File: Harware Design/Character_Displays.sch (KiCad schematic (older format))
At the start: 53 parts, among them P10 CONN_01X01, P11 CONN_01X01, P12 CONN_01X01, P13 CONN_01X04, P14 CONN_01X01, P15 CONN_01X01, P17 CONN_01X16, P18 CONN_01X16, P20 CONN_01X01, P21 CONN_01X08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

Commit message: Changed design files as per issues
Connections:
- net MISO: now also SD1.7 (DATA0); no longer U5.3 (1Y)
- net at U5.2 (1A): no longer SD1.7 (DATA0)
- no-connect marks 8 -> 10
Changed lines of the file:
@@
 Text GLabel 5900 3850 0    40   Input ~ 0
 SCK
-Wire Wire Line
-	7900 4100 7600 4100
-Wire Wire Line
-	7600 4100 7600 4500
-Wire Wire Line
-	7600 4500 5650 4500
-Wire Wire Line
-	5650 3550 6000 3550
-Text GLabel 5900 3650 0    40   Input ~ 0
+Text GLabel 7900 4100 0    40   Input ~ 0
 MISO
 $Comp
@@
 	6900 3550 6800 3550
 Connection ~ 6900 3850
-Wire Wire Line
-	5900 3650 6000 3650
 Wire Wire Line
 	5950 3450 6000 3450
@@
 Wire Wire Line
 	7050 3350 7050 3400
-Wire Wire Line
-	5650 4500 5650 3550
 $Comp
 L CONN_01X01 P20
@@
 $EndComp
 NoConn ~ 7700 6250
+NoConn ~ 6000 3550
+NoConn ~ 6000 3650
 $EndSCHEMATC

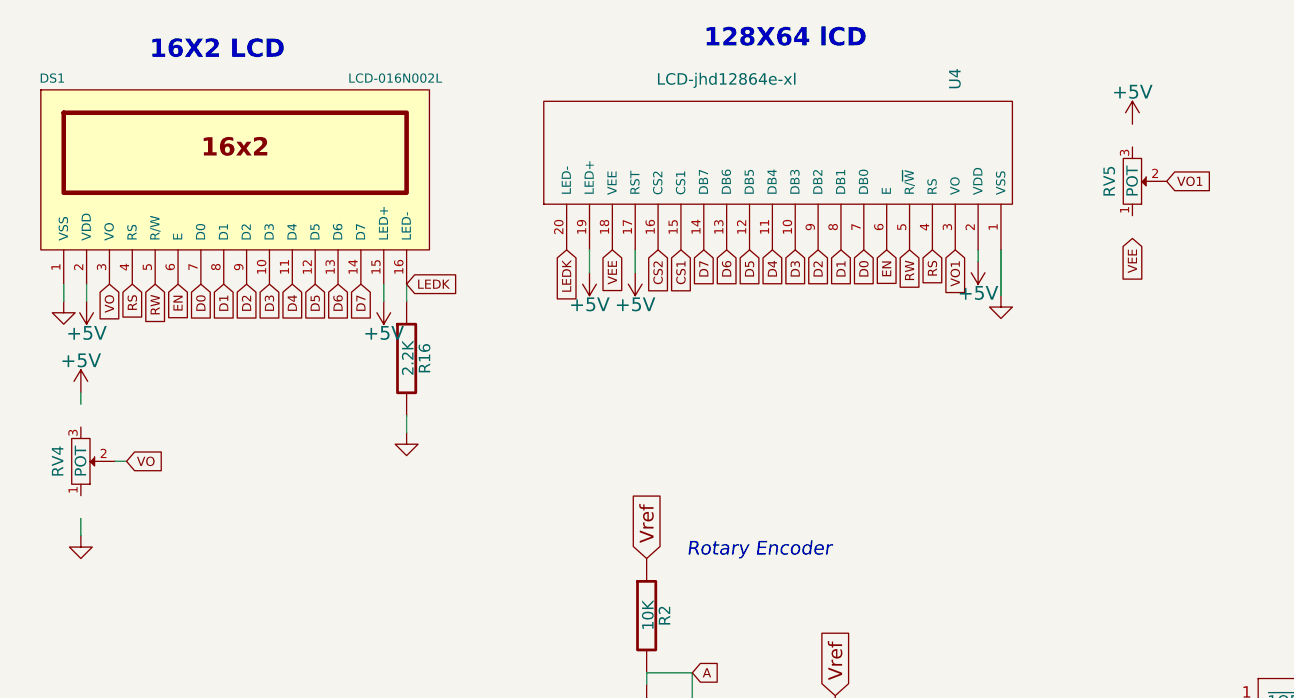
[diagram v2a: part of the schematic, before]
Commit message: RGB LED and D4 footprints are changed
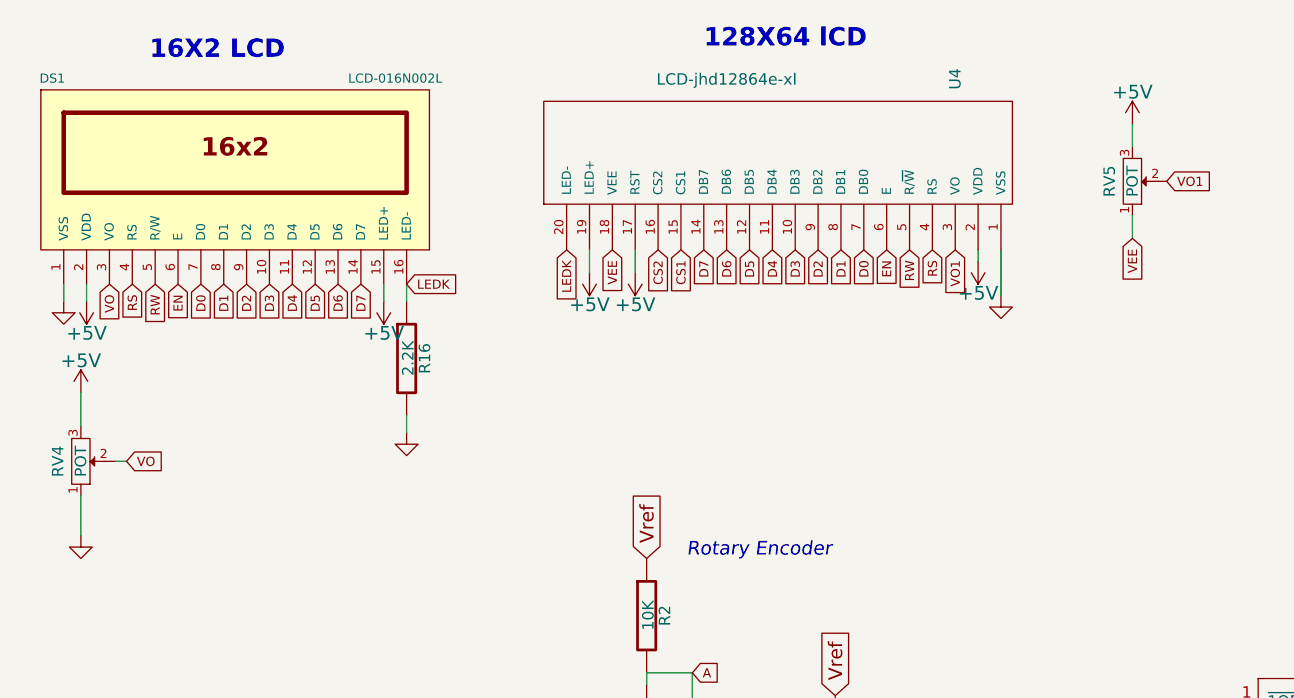
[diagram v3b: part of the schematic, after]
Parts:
- BT1: footprint (none) -> EE:VRT Cell holder
- C1, C2, C7, C8: footprint (none) -> Capacitors_SMD:C_0603_HandSoldering
- D10, D11, D12, D13, D5, D6, D7, D8: footprint (none) -> EE:LED-0603_NEW
- DS1: footprint (none) -> Display:WC1602A
- P10, P11, P12, P14: footprint (none) -> EE:M3_mounting
- P13: footprint (none) -> Pin_Headers:Pin_Header_Straight_1x04
- P15: footprint (none) -> Logo_New:Logo_10
- P17, P18: footprint (none) -> Pin_Headers:Pin_Header_Straight_1x16
- P20: footprint (none) -> Logo_New:Logo_16
- P21: footprint (none) -> Pin_Headers:Pin_Header_Straight_1x08
- R16, R17, R18, R19, R2, R20, R21, R22, R23, R29, R3, R30, R31, R32, R33, R34, R35, R36, R4: footprint (none) -> Resistors_SMD:R_0603_HandSoldering
- RV4, RV5: footprint (none) -> EE:TrimPOT_WithKnob
- SD1: footprint (none) -> EE:Micro_SD
- U1, U7: footprint (none) -> Housings_SOIC:SOIC-8_3.9x4.9mm_Pitch1.27mm
- U3: footprint (none) -> WRGB:sfh5712
- U4: footprint (none) -> Pin_Headers:Pin_Header_Straight_1x20
- U5: footprint (none) -> Housings_SSOP:SSOP-14_5.3x6.2mm_Pitch0.65mm
- U9: footprint (none) -> Rotary_Encoder:encoder_alps-ec12d
- X1: footprint (none) -> EE:RTC_Crystal_1
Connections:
- net +5V: now also RV4.3, RV5.3
- net GND: now also RV4.1
- net VEE: now also RV5.1

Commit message: Schematic for 7Segment and other added
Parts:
- DS1: symbol LCD-016N002L -> LCD-016N002L-RESCUE-One_Base_Board
- RV4, RV5: symbol POT -> POT-RESCUE-One_Base_Board
- U9: symbol Rotary_Encoder -> Rotary_Encoder-RESCUE-One_Base_Board
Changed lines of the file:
@@
 LIBS:memory
 LIBS:xilinx
-LIBS:special
 LIBS:microcontrollers
 LIBS:dsp
@@
 $EndDescr
 $Comp
-L LCD-016N002L DS1
+L LCD-016N002L-RESCUE-One_Base_Board DS1
 U 1 1 56EF4D06
 P 1625 1125
+AR Path="/56EF4D06" Ref="DS1"  Part="1"
+AR Path="/5526298B/56EF4D06" Ref="DS1"  Part="1"
 F 0 "DS1" H 825 1525 40  0000 C CNN
 F 1 "LCD-016N002L" H 2325 1525 40  0000 C CNN
@@
 LEDK
 $Comp
-L POT RV4
+L POT-RESCUE-One_Base_Board RV4
 U 1 1 56EF4D38
 P 950 2400
@@
 $EndComp
 $Comp
-L POT RV5
+L POT-RESCUE-One_Base_Board RV5
 U 1 1 56EF4D68
 P 5550 1175
@@
 VBAT
 $Comp
-L Rotary_Encoder U9
+L Rotary_Encoder-RESCUE-One_Base_Board U9
 U 1 1 57BC7B5B
 P 3875 4075
